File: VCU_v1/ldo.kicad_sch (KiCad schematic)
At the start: 3 parts, among them U2 AMS1117-3.3

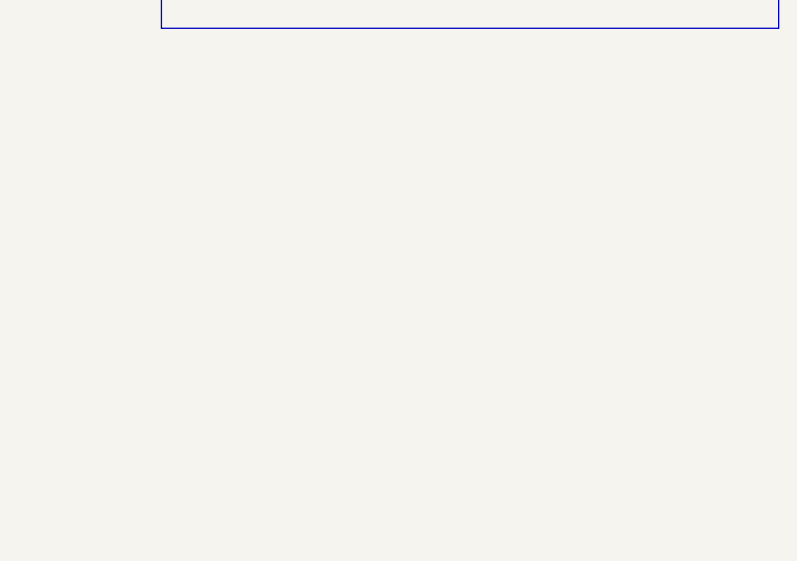
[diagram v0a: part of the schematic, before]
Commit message: added rpp, pedal buffer/low pass, can transceivers, began connector pinout
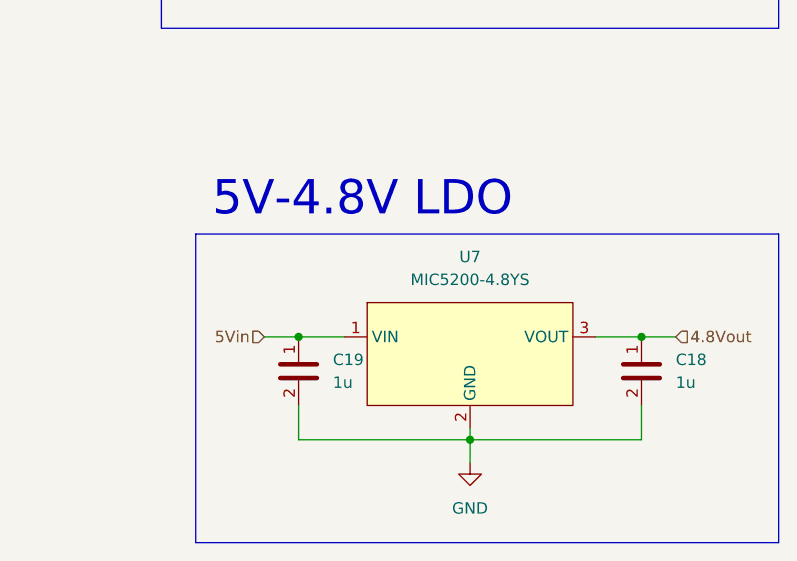
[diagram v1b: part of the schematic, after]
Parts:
- added C18, C19: 1u, Capacitor_SMD:C_0603_1608Metric_Pad1.08x0.95mm_HandSolder, symbol BFR Capacitors:CL10A105KB8NNNC
- added U7: MIC5200-4.8YS, symbol MIC5200-LDO:MIC5200-4.8YS
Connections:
- net 5Vin: now also C19.1, U7.1 (VIN)
- net GND: now also C18.2, C19.2, U7.2 (GND)
- new net 4.8Vout: C18.1, U7.3 (VOUT)
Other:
- note added: "5V-4.8V LDO"

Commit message: p dih r
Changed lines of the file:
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@@
 		(on_board yes)
 		(dnp no)
-		(fields_autoplaced yes)
 		(property "Reference" "C19"
-			(at 110.49 113.0299 0)
+			(at 109.728 113.03 0)
 			(effects
 				(font
@@
 		)
 		(property "Value" "1u"
-			(at 110.49 115.5699 0)
+			(at 109.728 115.57 0)
 			(effects
 				(font

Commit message: v1 schematic (actually) complete, let the layout commence
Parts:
- added TP3, TP4: RH-5015, TestPoint:TestPoint_Keystone_5015_Micro_Mini, symbol .Test-Point:RH-5015
- U4: renamed from U7; footprint (none) -> Package_TO_SOT_SMD:SOT-223-3_TabPin2
- renumbered C19 to C14, C8 to C15, C9 to C16, C18 to C17, U2 to U3
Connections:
- net 3.3Vout: now also TP3.1
- net 4.8Vout: now also TP4.1

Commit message: omids wisdom came all over my power converters
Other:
- moved on the sheet: C14, C17, TP4, U4

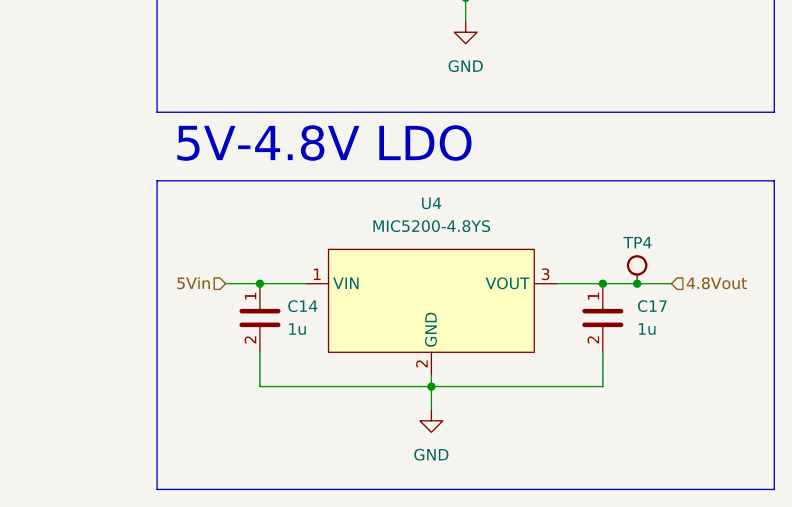
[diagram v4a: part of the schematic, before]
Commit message: fixing drc errors, done besides that
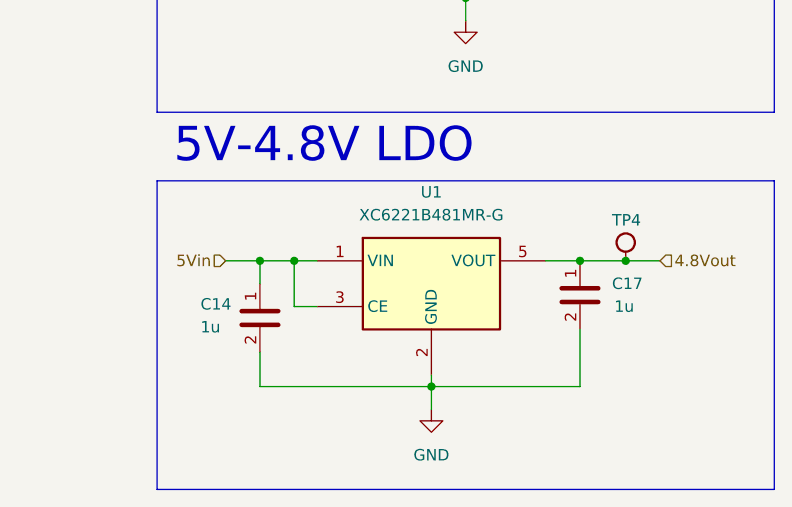
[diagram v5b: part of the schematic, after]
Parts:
- removed U4: MIC5200-4.8YS, Package_TO_SOT_SMD:SOT-223-3_TabPin2, symbol MIC5200-LDO:MIC5200-4.8YS
- added U1: XC6221B481MR-G, Package_TO_SOT_SMD:SOT-23-5, symbol Regulator_Linear:XC6220B331MR
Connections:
- net 4.8Vout: now also U1.5 (VOUT)
- net 5Vin: now also U1.1 (VIN), U1.3 (CE)
- net GND: now also U1.2 (GND)
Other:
- moved on the sheet: C17, TP4
